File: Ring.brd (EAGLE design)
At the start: 100 x 80 mm, 23 parts, among them U1 BQ25125YFPR, U3 NRF52832-CIAA-R

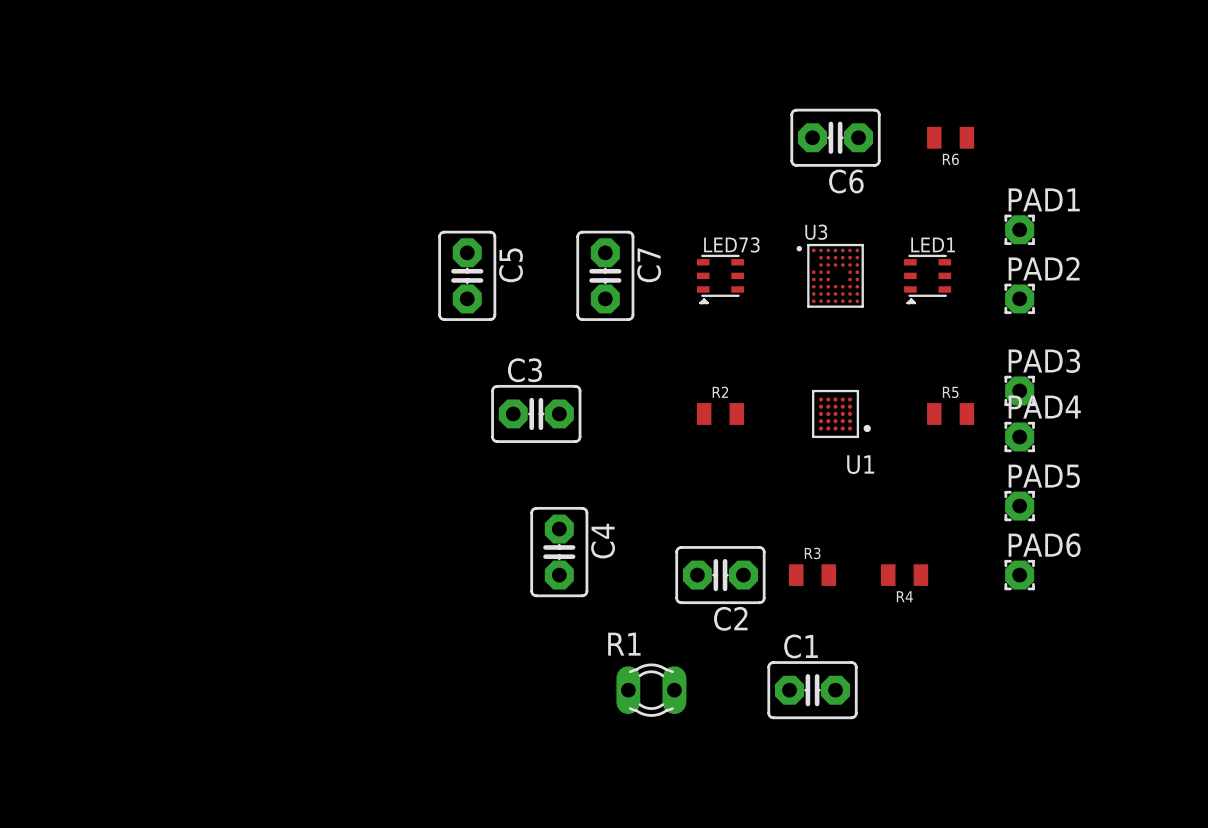
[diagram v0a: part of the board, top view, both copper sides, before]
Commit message: Created New schemtatic
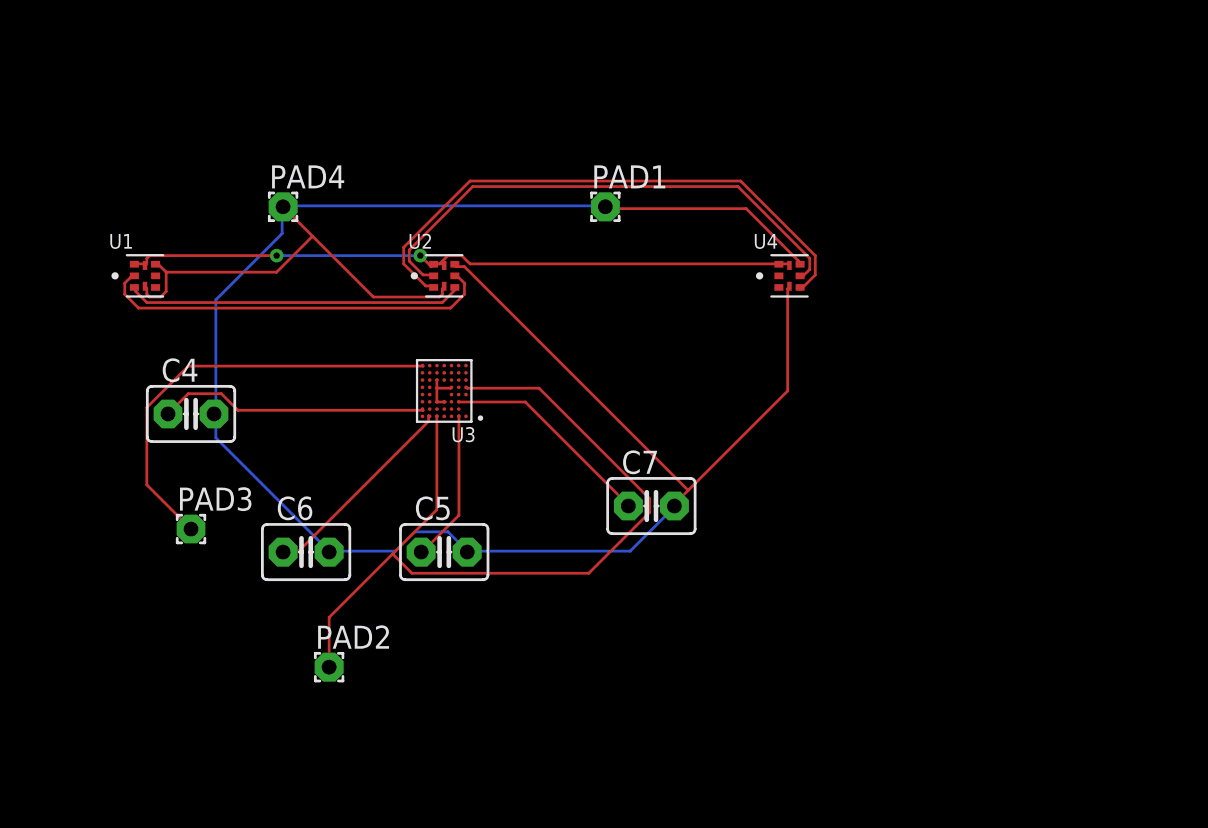
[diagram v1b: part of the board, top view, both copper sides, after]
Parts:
- removed C1, C2: 1 microF, capacitor-wima:C2.5-3
- removed C3: 10 microF, capacitor-wima:C2.5-3
- removed LED1, LED73: (no value), microbuilder:APA102_2020
- removed PAD5, PAD6: (no value), wirepad:1,6/0,8
- removed R1: (no value), ptc-ntc:P640
- removed R2, R3, R4, R5, R6: 0.3, SparkFun-Resistors:0805
- added U2, U4: APA-102-2020-256-8, APA-102-2020-256-8:LED_APA-102-2020-256-8
- U1: value BQ25125YFPR -> APA-102-2020-256-8; device BQ25125YFPR:BGA25N40P5X5_253X247X50N -> APA-102-2020-256-8:LED_APA-102-2020-256-8
- moved PAD3 46.4 mm to (11.4, 30.5)
- moved PAD2 43.2 mm to (19.1, 22.9)
- moved PAD4 42.6 mm to (16.5, 48.3)
- moved U1 38.9 mm to (8.89, 44.5), turned to 0 degrees
- moved C6 37.1 mm to (17.8, 29.2), turned to 0 degrees
- moved PAD1 22.9 mm to (34.3, 48.3)
- moved U3 22.5 mm to (25.4, 38.1), turned to 180 degrees
- moved C4 21.7 mm to (11.4, 36.8), turned to 0 degrees
- moved C5 15.3 mm to (25.4, 29.2), turned to 0 degrees
- moved C7 13.0 mm to (36.8, 31.8), turned to 0 degrees
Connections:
- removed net N$1: LED1.6, LED73.1
- removed net N$10: U1.E5, U3.G3
- removed net N$11: U1.D2, U3.F3
- removed net N$12: U1.D3, U3.G7
- removed net N$13: C2.1, R3.2, U1.A2
- removed net N$14: R2.2, U1.C3
- removed net N$16: U1.A4
- removed net N$17: R5.2, U1.C1
- removed net N$19: R6.2, U1.D1
- removed net N$24: PAD5.1, U1.A3, U1.B3
- removed net N$25: PAD6.1, U1.D4
- removed net N$3: LED1.5, LED73.2
- removed net N$9: U1.E4, U3.G4
- net GND: now also U1.5_1, U1.5_2, U2.5_1, U2.5_2, U4.5_1, U4.5_2; no longer C1.2, C2.2, C3.2, LED1.4, LED73.4, R1.1, R2.1, R3.1, R4.1, R5.1, R6.1, U1.A1, U1.A5, U1.D5
- net N$15: now also U3.A5
- net N$18: no longer C3.1, U1.B4, U1.B5, U1.C4
- net N$2: now also U1.1, U2.3; no longer R4.2, U1.C2
- net N$4: now also U1.3; no longer LED73.6
- net N$5: now also U1.6; no longer LED73.5
- net N$6: now also U1.4, U2.6; no longer C1.1, R1.2, U1.B1, U1.B2
- net N$7: now also U2.1, U4.3; no longer U1.E2, U3.H6
- net N$8: now also U2.4, U4.6; no longer U1.E3, U3.F4
- net VCC: now also U1.2_1, U1.2_2, U2.2_1, U2.2_2, U4.2_1, U4.2_2; no longer LED1.3, LED73.3
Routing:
- net GND: track 0.00 -> 133.6 mm
- net N$15: track 0.00 -> 45.8 mm
- net VCC: track 0.00 -> 37.6 mm, vias 0 -> 2
- net N$8: track 0.00 -> 31.3 mm
- net N$7: track 0.00 -> 28.9 mm
- net N$18: track 0.00 -> 23.9 mm
- net N$2: track 0.00 -> 22.0 mm
- net N$6: track 0.00 -> 18.6 mm
- net N$20: track 0.00 -> 15.0 mm
- net N$22: track 0.00 -> 11.8 mm
- net N$23: track 0.00 -> 11.4 mm
- net N$21: track 0.00 -> 8.43 mm

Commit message: projects added
added projects
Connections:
- net N$15: no longer U3.A5
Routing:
- net N$15: track 45.8 -> 43.0 mm
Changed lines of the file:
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@@
 <signal name="N$15">
 <contactref element="U3" pad="E1"/>
-<contactref element="PAD2" pad="1"/>
-<contactref element="U3" pad="A5"/>
 <wire x1="24.9936" y1="31.5468" x2="24.9936" y2="36.7284" width="0.1524" layer="1"/>
 <wire x1="19.05" y1="25.6032" x2="22.5552" y2="29.1084" width="0.1524" layer="1"/>
 <wire x1="22.5552" y1="29.1084" x2="24.9936" y2="31.5468" width="0.1524" layer="1"/>
-<wire x1="19.05" y1="22.86" x2="19.05" y2="25.6032" width="0.1524" layer="1"/>
-<wire x1="24.9936" y1="36.7284" x2="25" y2="36.7" width="0.1524" layer="1"/>
 <wire x1="30.6324" y1="38.2524" x2="26.67" y2="38.2524" width="0.1524" layer="1"/>
 <wire x1="36.7284" y1="32.1564" x2="30.6324" y2="38.2524" width="0.1524" layer="1"/>
@@
 <wire x1="22.5552" y1="29.1084" x2="23.622" y2="28.0416" width="0.1524" layer="1"/>
 <wire x1="26.67" y1="38.2524" x2="26.6" y2="38.3" width="0.1524" layer="1"/>
+<contactref element="PAD2" pad="1"/>
+<wire x1="19.05" y1="22.86" x2="19.05" y2="25.6032" width="0" layer="19" extent="1-1"/>
 </signal>
 <signal name="N$18">
